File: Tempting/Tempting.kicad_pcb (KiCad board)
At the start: 4 copper layers, 52.9 x 65 mm, 62 parts, among them J1 Conn_Coaxial, J2 Conn_01x07_Socket, J3 Conn_ARM_SWD_TagConnect_TC2030, J4 USB_C_Receptacle_USB2.0_16P, SW1 SPST, SW2 SPST, U1 AMS1117-3.3, U2 SCD41-D-R2, U3 STM32WB55CGUx, U4 DPS368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

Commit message: Updated gerbers
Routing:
- net +3.3V: track 218.5 -> 219.6 mm
- net /OLED_CLK: track 33.3 -> 34.3 mm
- net /OLED_NCS: track 29.1 -> 30.1 mm
- net /OLED_DIN: track 31.0 -> 31.9 mm
- net /OLED_DC: track 22.8 -> 23.5 mm
- net /OLED_NRST: track 29.1 -> 29.7 mm

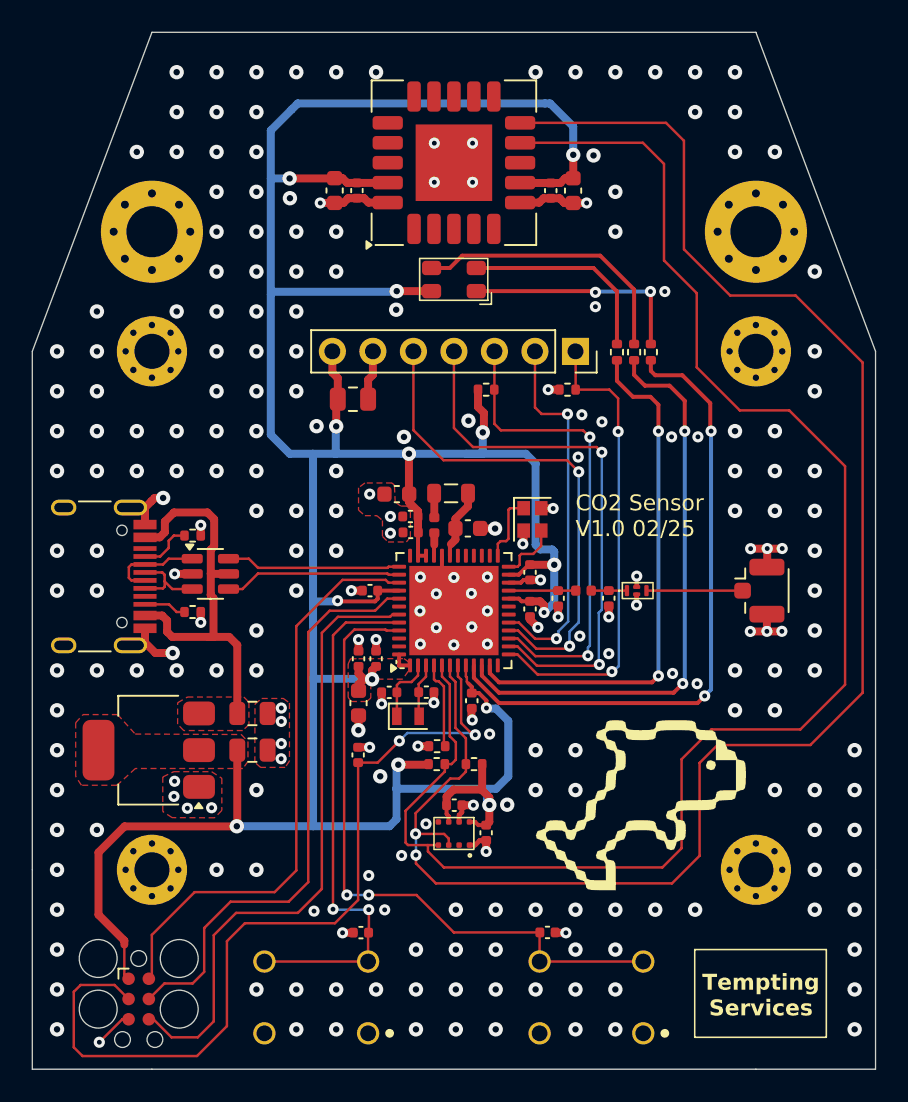
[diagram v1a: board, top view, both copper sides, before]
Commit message: Updated ufl connector to sma
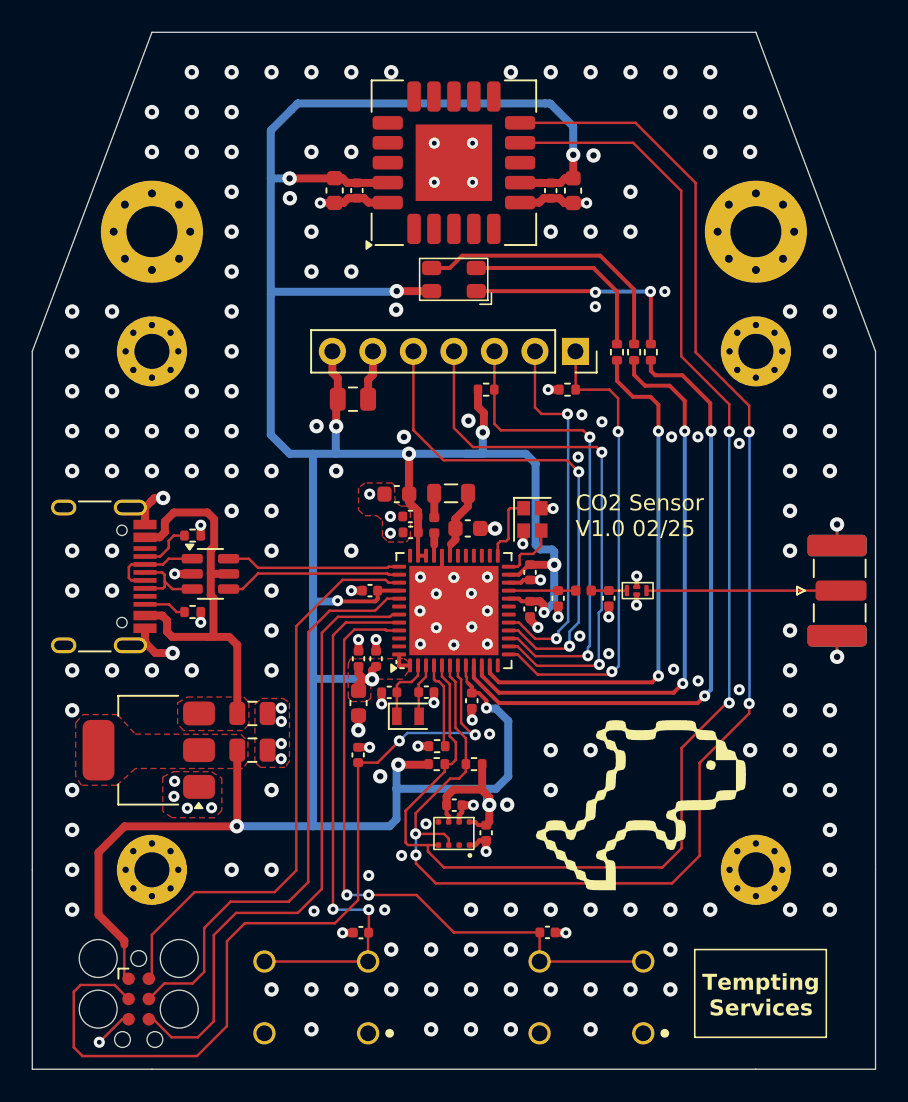
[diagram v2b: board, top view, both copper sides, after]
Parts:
- C11, C15: value C -> 10p
- J1: footprint Connector_Coaxial:U.FL_Hirose_U.FL-R-SMT-1_Vertical -> Connector_Coaxial:SMA_Samtec_SMA-J-P-H-ST-EM1_EdgeMount
- moved J1 5.12 mm to (181.6, 95.0)
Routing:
- net /SENSORS_SDA: track 106.3 -> 93.5 mm, vias 2 -> 4
- net /SENSORS_SCL: track 98.8 -> 87.6 mm, vias 0 -> 2
- net /RF_COAX_LPF: track 6.03 -> 12.1 mm
- net GND: track 53.0 -> 52.0 mm, vias 247 -> 220
